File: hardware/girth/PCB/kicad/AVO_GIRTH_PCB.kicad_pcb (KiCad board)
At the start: 4 copper layers, 65.5 x 43.5 mm, 115 parts, among them J1 USB-C 16P, J2 BATERÍA 1S, K1 G6KU-2F-Y DC3, Q1 AO3401A, Q10 AO3401A, Q11 AO3400A, Q12 2N7002, Q13 AO3400A, Q14 AO3401A, Q15 2N7002, Q16 2N7002, Q2 AO3401A, Q3 AO3401A, SW1 REED (1), SW2 REED (2), U1 BQ51013BRHLR, U2 BQ24072RGTR, U3 RT9080-33GJ5, U4 ESP32-C6-MINI-1U-N4, U5 BNO085, U6 USBLC6-2SC6, Y1 32,768 kHz 12,5 pF

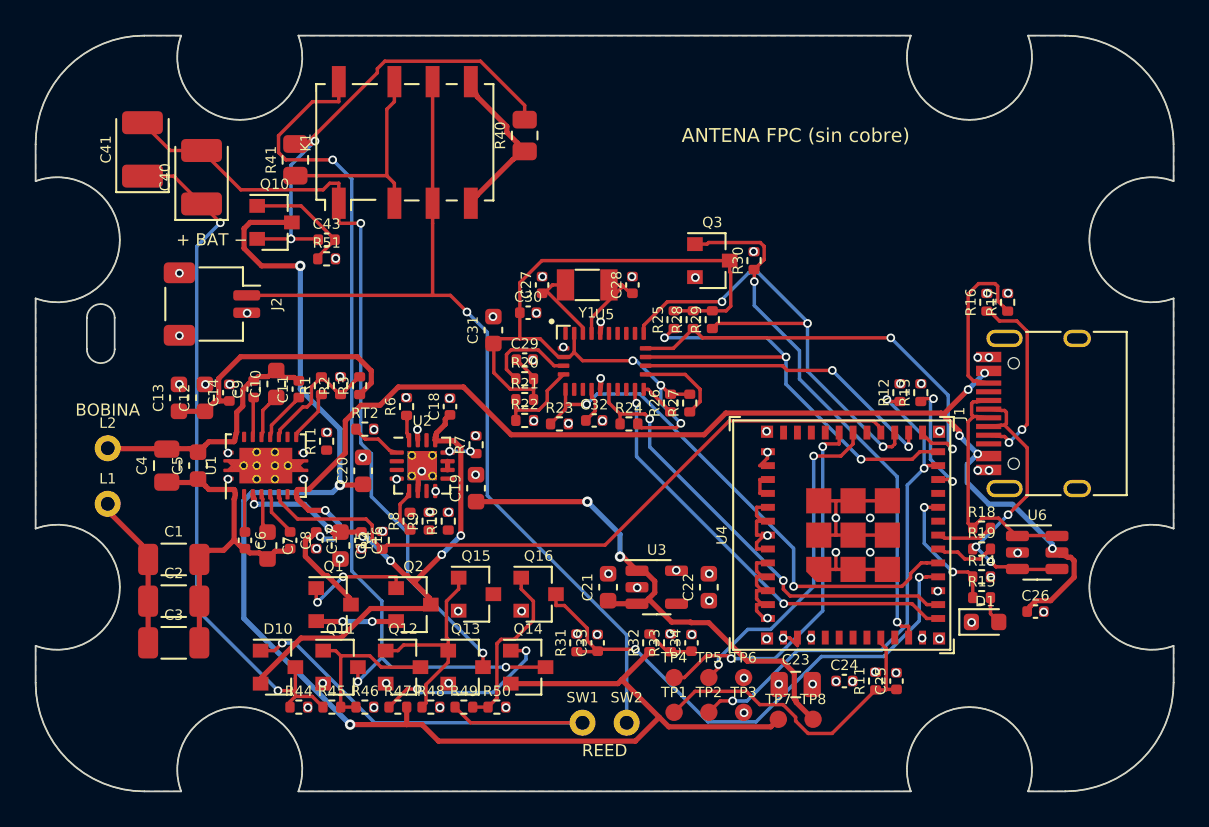
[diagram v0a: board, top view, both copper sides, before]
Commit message: PCB cincha: DRC/ERC, Gerber y renders de KiCad 9 [skip ci]
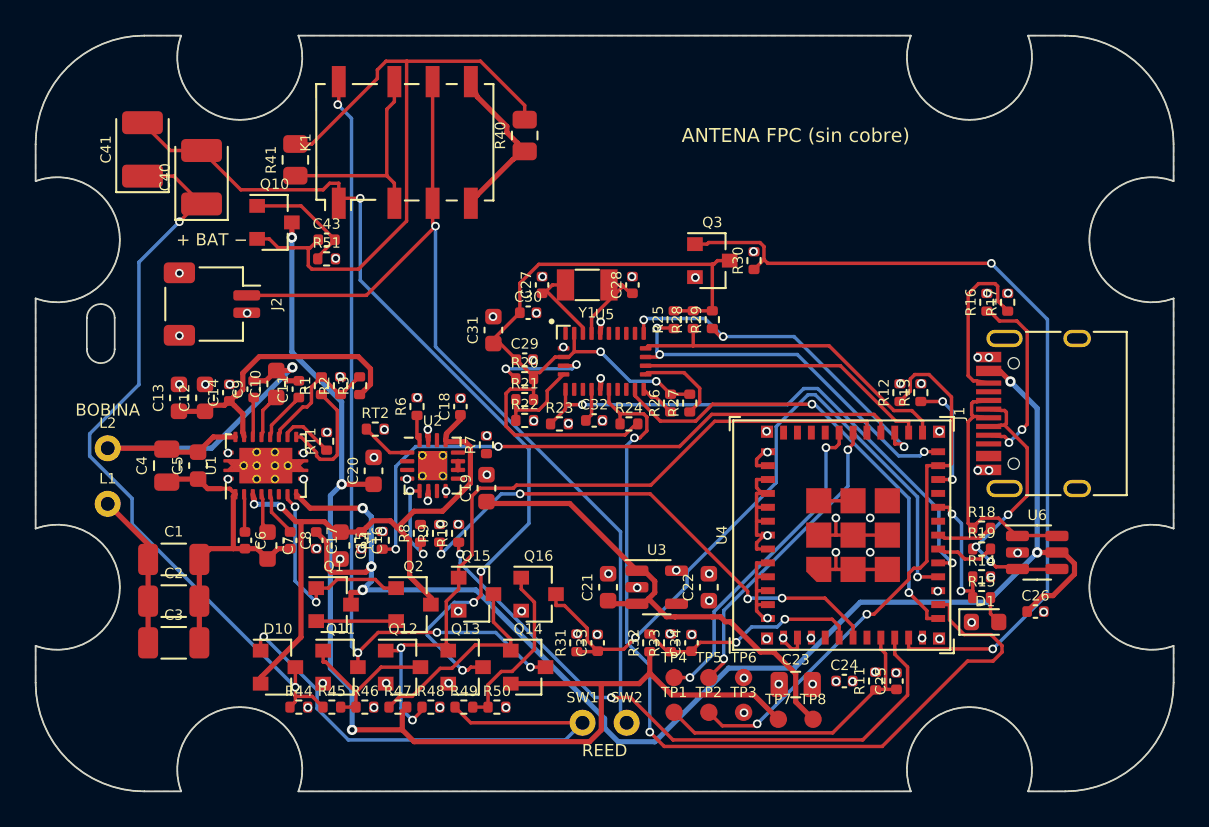
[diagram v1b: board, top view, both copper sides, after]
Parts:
- moved R8 0.92 mm to (89.4, 106.9)
- moved R10 0.92 mm to (91.6, 106.9)
- moved R9 0.92 mm to (90.5, 106.9)
- moved C18 0.60 mm to (91.7, 99.6)
- moved C19 0.60 mm to (93.2, 104.3)
- moved C20 0.60 mm to (86.7, 103.3)
- moved R6 0.60 mm to (89.2, 99.6)
- moved R7 0.60 mm to (93.2, 101.8)
- moved RT2 0.60 mm to (86.8, 100.9)
- moved U2 0.60 mm to (90.1, 103.0)
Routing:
- net CHG_STAT: track 0.00 -> 35.9 mm, vias 0 -> 2
- net RLY_OFF: track 12.1 -> 43.9 mm, vias 0 -> 2
- net CHG_PG: track 0.00 -> 30.0 mm, vias 0 -> 4
- net IMU_RST: track 26.3 -> 51.6 mm
- net IMU_PWR_N: track 30.8 -> 49.2 mm
- net VBAT: track 82.8 -> 70.0 mm
- net BAT_SW: track 27.8 -> 38.4 mm, vias 2 -> 0
- net BAT_ADC: track 2.83 -> 12.9 mm, vias 0 -> 2
- net QI_AC2: track 14.6 -> 24.5 mm, vias 0 -> 1
- net REED: track 32.1 -> 40.9 mm
- net IMU_MISO: track 28.4 -> 20.9 mm
- net K_A: track 45.1 -> 51.8 mm, vias 2 -> 4
- net IMU_CS: track 28.6 -> 22.0 mm
- net QI_ADEN: track 6.63 -> 12.7 mm
- net K_B: track 51.9 -> 46.3 mm, vias 3 -> 4
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
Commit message: PCB cincha: DRC/ERC, Gerber y renders de KiCad 9 [skip ci]
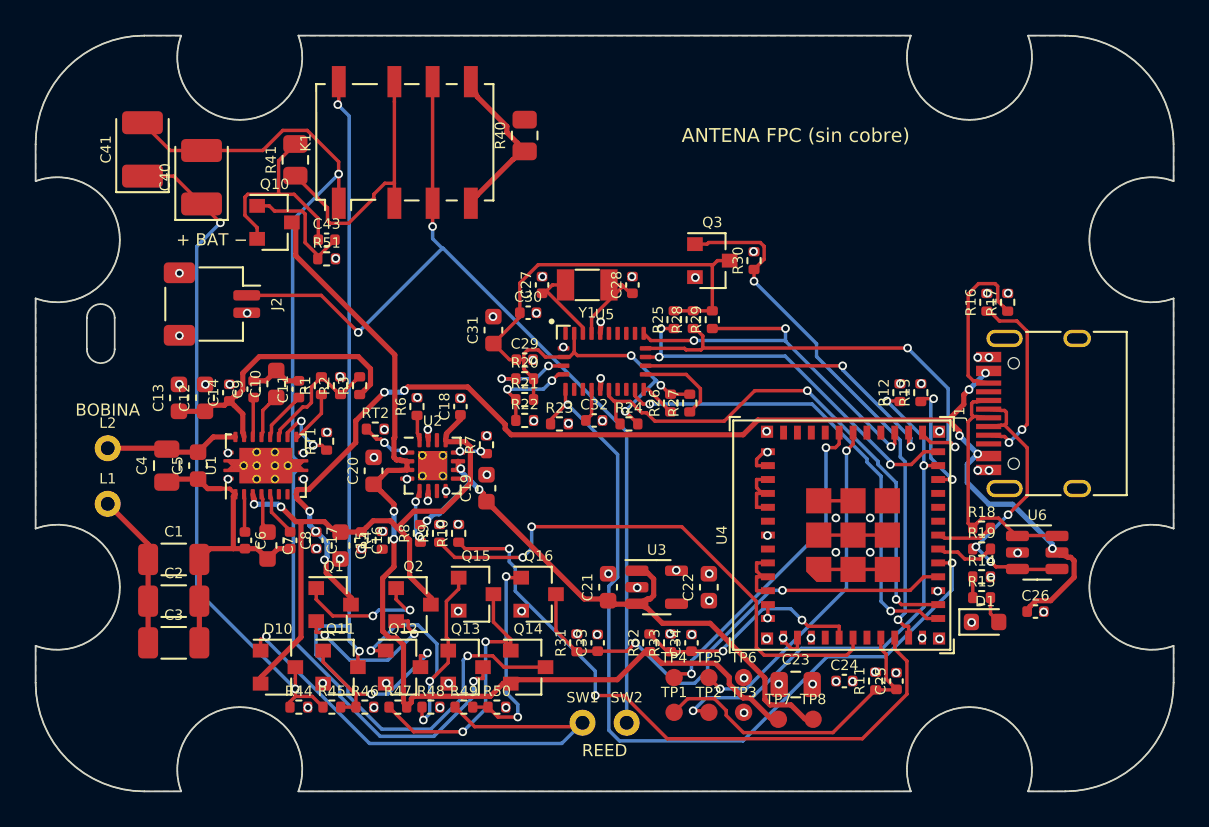
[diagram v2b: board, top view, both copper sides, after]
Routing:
- net QI_CHG: track 35.5 -> 0.00 mm, vias 2 -> 0
- net BAT_SW: track 38.4 -> 12.1 mm
- net RLY_OFF: track 43.9 -> 17.9 mm, vias 2 -> 3
- net IMU_RST: track 51.6 -> 31.2 mm
- net IMU_PWR_N: track 49.2 -> 31.0 mm
- net IMU_WAKE: track 31.3 -> 48.6 mm
- net QI_AC2: track 24.5 -> 10.9 mm, vias 1 -> 0
- net REED: track 40.9 -> 28.9 mm
- net VBAT: track 70.0 -> 58.6 mm, vias 3 -> 2
- net K_B: track 46.3 -> 56.2 mm, vias 4 -> 3
- net VBUS: track 81.7 -> 73.1 mm, vias 5 -> 10
- net GND: track 41.3 -> 33.0 mm
- net K_A: track 51.8 -> 59.8 mm, vias 4 -> 2
- net IMU_VDD: track 49.4 -> 42.1 mm, vias 2 -> 3
- net LED: track 7.64 -> 1.20 mm, vias 2 -> 0
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
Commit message: PCB cincha: resultados de KiCad 9 de bc3cb27 (puerta: false) [skip ci]
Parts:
- added D11: BAT54C, AVO:SOT-23, F.Cu at (94.1, 91.2)
- added Q17: AO3401A, AVO:SOT-23, F.Cu at (87.1, 91.2)
- added Q18: 2N7002, AVO:SOT-23, F.Cu at (90.6, 91.2)
- added R52: 10R, AVO:R_0805_2012Metric, F.Cu at (85.4, 94.0)
- added R53: 100k, AVO:R_0402_1005Metric, F.Cu at (88.2, 93.8)
- added R54: 100k, AVO:R_0402_1005Metric, F.Cu at (90.2, 93.8)
- added R55: 1k, AVO:R_0402_1005Metric, F.Cu at (91.7, 94.4)
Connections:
- U4 pad 19: (no net) -> RLY_ON
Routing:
- net RLY_GB: track 11.2 -> 59.2 mm, vias 2 -> 3
- net RLY_ON: track 0.00 -> 39.4 mm, vias 0 -> 2
- net BAT_SW: track 12.1 -> 33.0 mm
- net K_A: track 59.8 -> 78.7 mm, vias 2 -> 5
- net IMU_RST: track 31.2 -> 46.5 mm
- net VSYS: track 34.8 -> 50.0 mm, vias 3 -> 0
- net RLY_SG: track 0.00 -> 12.9 mm, vias 0 -> 2
- net GND: track 33.0 -> 45.7 mm, vias 80 -> 74
- net GPIO8: track 6.85 -> 19.6 mm
- net BOOT: track 31.0 -> 40.6 mm
- net AD_SRC: track 9.16 -> 0.00 mm, vias 2 -> 0
- net REED_HI: track 30.3 -> 24.0 mm, vias 1 -> 2
- net LED: track 1.20 -> 7.42 mm, vias 0 -> 2
- net K_A_SET: track 0.00 -> 5.98 mm, vias 0 -> 2
- net EN: track 18.5 -> 24.3 mm
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
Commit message: PCB cincha: resultados de KiCad 9 de 8f7eaff (puerta: false) [skip ci]
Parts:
- moved C28 0.30 mm to (101.9, 92.6)
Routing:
- net RLY_OFF: track 17.9 -> 61.2 mm, vias 3 -> 4
- net RLY_GB: track 59.2 -> 83.9 mm
- net K_A: track 78.7 -> 54.8 mm, vias 5 -> 3
- net GPIO8: track 19.6 -> 10.6 mm
- net AD_SRC: track 0.00 -> 7.39 mm, vias 0 -> 2
- net IMU_RST: track 46.5 -> 40.0 mm
- net BAT_RAW: track 55.7 -> 60.1 mm
- net IMU_ENV_SCL: track 4.27 -> 8.28 mm
- net GND: track 45.7 -> 42.7 mm
- net IMU_MISO: track 22.8 -> 20.9 mm
- net IMU_MOSI: track 18.9 -> 18.4 mm

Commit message: PCB cincha: resultados de KiCad 9 de b3097be (puerta: false) [skip ci]
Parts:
- moved C6 2.42 mm to (78.1, 109.4)
- moved C8 2.42 mm to (80.7, 109.4)
- moved C7 2.33 mm to (79.4, 109.6)
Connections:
- D11 pad 2: (no net) -> unconnected-(D11-A2-Pad2)
- J1 pad A8: (no net) -> unconnected-(J1-SBU1-PadA8)
- J1 pad B8: (no net) -> unconnected-(J1-SBU2-PadB8)
- U2 pad 14: (no net) -> unconnected-(U2-TMR-Pad14)
- U3 pad 4: (no net) -> unconnected-(U3-NC-Pad4)
- U4 pad 21: (no net) -> unconnected-(U4-NC-Pad21)
- U4 pad 32: (no net) -> unconnected-(U4-NC-Pad32)
- U4 pad 33: (no net) -> unconnected-(U4-NC-Pad33)
- U4 pad 34: (no net) -> unconnected-(U4-NC-Pad34)
- U4 pad 35: (no net) -> unconnected-(U4-NC-Pad35)
- U4 pad 4: (no net) -> unconnected-(U4-NC-Pad4)
- U4 pad 7: (no net) -> unconnected-(U4-NC-Pad7)
- U5 pad 1: (no net) -> unconnected-(U5-NC-Pad1)
- U5 pad 12: (no net) -> unconnected-(U5-NC-Pad12)
- U5 pad 13: (no net) -> unconnected-(U5-NC-Pad13)
- U5 pad 21: (no net) -> unconnected-(U5-NC-Pad21)
- U5 pad 22: (no net) -> unconnected-(U5-NC-Pad22)
- U5 pad 23: (no net) -> unconnected-(U5-NC-Pad23)
- U5 pad 24: (no net) -> unconnected-(U5-NC-Pad24)
- U5 pad 7: (no net) -> unconnected-(U5-NC-Pad7)
- U5 pad 8: (no net) -> unconnected-(U5-NC-Pad8)
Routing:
- net +3V3: track 0.47 -> 90.3 mm, vias 15 -> 6
- net RLY_GB: track 83.9 -> 41.6 mm, vias 3 -> 4
- net QI_CHG: track 0.00 -> 40.1 mm, vias 0 -> 2
- net IMU_WAKE: track 50.2 -> 30.6 mm
- net REED_G: track 13.6 -> 0.88 mm, vias 2 -> 0
- net IMU_RST: track 40.0 -> 29.1 mm, vias 2 -> 3
- net IMU_SCK: track 23.9 -> 34.3 mm
- net QI_AC2: track 10.9 -> 20.6 mm
- net BOOT: track 40.5 -> 31.1 mm
- net IMU_VDD: track 44.1 -> 34.9 mm, vias 2 -> 4
- net K_B: track 52.9 -> 61.6 mm
- net GND: track 42.7 -> 50.4 mm
- net RLY_OFF: track 61.2 -> 54.1 mm
- net QI_ILIM: track 6.98 -> 0.00 mm
- net IMU_INT: track 24.6 -> 31.4 mm
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
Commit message: PCB cincha: resultados de KiCad 9 de 7f80a18 (puerta: false) [skip ci]
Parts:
- moved C15 7.46 mm to (78.7, 111.9), turned to 0 degrees
- moved C16 6.72 mm to (81.1, 111.9), turned to 0 degrees
- moved J2 1.60 mm to (75.8, 93.7)
- moved C10 1.60 mm to (81.1, 96.7)
- moved C11 1.60 mm to (82.4, 97.0)
- moved C9 1.60 mm to (79.8, 97.0)
- moved C6 0.50 mm to (77.6, 109.4)
- moved C1 0.40 mm to (74.8, 108.4)
- moved C2 0.40 mm to (74.8, 110.8)
- moved C3 0.40 mm to (74.8, 113.2)
- moved C8 0.10 mm to (80.6, 109.4)
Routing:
- net K_B: track 61.6 -> 45.3 mm
- net VIN5: track 28.8 -> 40.1 mm, vias 4 -> 2
- net REED_G: track 0.88 -> 11.1 mm, vias 0 -> 2
- net IMU_VDD: track 34.9 -> 41.5 mm, vias 4 -> 3
- net SS_G: track 7.08 -> 1.51 mm
- net IMU_SCK: track 34.3 -> 39.2 mm, vias 2 -> 3
- net BAT_ADC: track 17.3 -> 12.7 mm
- net IMU_INT: track 31.4 -> 27.1 mm
- net REED: track 29.7 -> 33.8 mm
- net IMU_CS: track 24.6 -> 20.7 mm, vias 3 -> 2
- net RLY_GB: track 41.6 -> 45.3 mm, vias 4 -> 3
- net IMU_MISO: track 24.3 -> 20.7 mm
- net CHG_STAT: track 36.1 -> 32.5 mm
- net AD_SRC: track 4.60 -> 8.14 mm, vias 0 -> 2
- net QI_TS: track 0.00 -> 3.21 mm
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
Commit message: PCB cincha: resultados de KiCad 9 de 05556bb (puerta: true) [skip ci]
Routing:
- net QI_ADEN: track 6.40 -> 11.6 mm
- net SS_G: track 1.51 -> 6.36 mm, vias 0 -> 2
- net QI_ILIM: track 0.00 -> 2.91 mm, vias 0 -> 2
- net VBUS: track 68.7 -> 68.2 mm
- net QI_CHG: vias 2 -> 4
